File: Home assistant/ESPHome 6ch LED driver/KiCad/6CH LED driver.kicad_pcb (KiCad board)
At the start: 2 copper layers, 90 x 70 mm, 75 parts, among them J1 DC Power, J10 I2C ext, J11 UART int, J12 UART ext, J13 IO Out, J14 U Out, J2 USB_C_small, J3 LED 1, J4 LED 2, J5 LED 3, J6 LED 4, J7 LED 5, J8 LED 6, J9 I2C int, Q1 AP4409AGEM, Q2 AP4409AGEM, Q3 AO3400A, Q4 AO3400A, Q5 AO3400A, Q6 AO3400A, Q7 AO3400A, Q8 AO3400A, SW1 Reset, SW2 Boot, U1 TPS5430DDA, U2 AMS1117-3.3, U3 ESP32-C6-WROOM-1

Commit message: Fix USB
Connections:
- R4 pad 1: USB D- -> USB D+
- R5 pad 1: USB D+ -> USB D-
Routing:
- net USB D-: track 25.0 -> 17.9 mm
- net USB D+: track 21.7 -> 18.9 mm
- net IO10: track 25.2 -> 24.2 mm
- net IO11: track 27.5 -> 26.5 mm
- net Net-(U3-MTDO/GPIO7): track 16.9 -> 16.3 mm

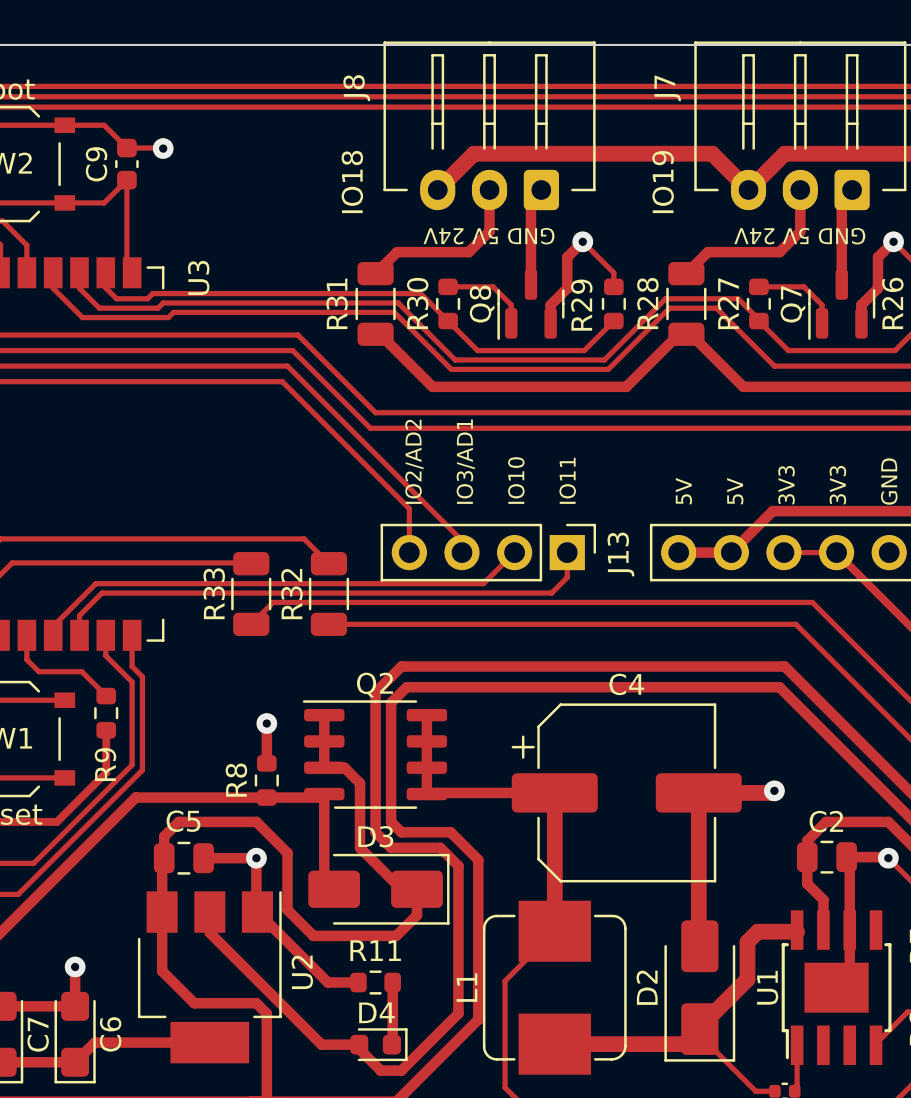
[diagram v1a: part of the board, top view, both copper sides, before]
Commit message: Fix boot mode
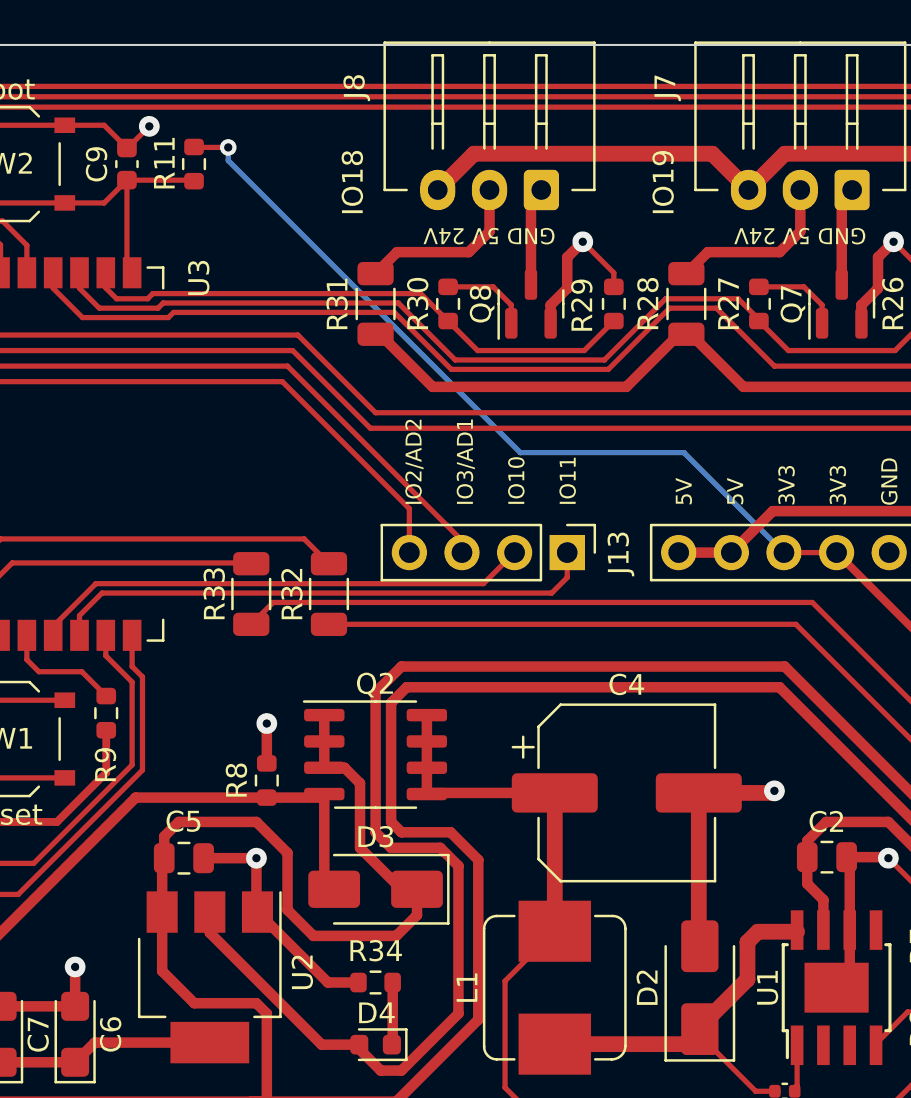
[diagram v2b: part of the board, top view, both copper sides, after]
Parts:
- added R11: 100k, Resistor_SMD:R_0603_1608Metric, F.Cu at (126.2, 68.8)
- renumbered R11 to R34
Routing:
- net +3V3: track 200.9 -> 237.9 mm, vias 0 -> 1
- net BOOT: track 14.0 -> 17.5 mm
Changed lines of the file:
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@@
     )
   )
+  (footprint "Resistor_SMD:R_0603_1608Metric" (layer "F.Cu")
+    (at 126.238 68.75 -90)
+    (descr "Resistor SMD 0603 (1608 Metric), square (rectangular) end terminal, IPC_7351 nominal, (Body size source: IPC-SM-782 page 72, https://www.pcb-3d.com/wordpress/wp-content/uploads/ipc-sm-782a_amendment_1_and_2.pdf), generated with kicad-footprint-generator")
+    (tags "resistor")
+    (property "Sheetfile" "6CH LED driver.kicad_sch")
+    (property "Sheetname" "")
+    (property "ki_description" "Resistor, small symbol")
+    (property "ki_keywords" "R resistor")
+    (attr smd)
+    (fp_text reference "R11" (at -0.043 1.397 90) (layer "F.SilkS")
+        (effects (font (size 1 1) (thickness 0.15)))
+    )
+    (fp_text value "100k" (at 0 1.43 90) (layer "F.Fab")
+        (effects (font (size 1 1) (thickness 0.15)))
+    )
+    (fp_text user "${REFERENCE}" (at 0 0 90) (layer "F.Fab")
+        (effects (font (size 0.4 0.4) (thickness 0.06)))
+    )
+    (fp_line (start -0.237258 -0.5225) (end 0.237258 -0.5225)
+      (stroke (width 0.12) (type solid)) (layer "F.SilkS"))
+    (fp_line (start -0.237258 0.5225) (end 0.237258 0.5225)
+      (stroke (width 0.12) (type solid)) (layer "F.SilkS"))
+    (fp_line (start -1.48 -0.73) (end 1.48 -0.73)
+      (stroke (width 0.05) (type solid)) (layer "F.CrtYd"))
+    (fp_line (start -1.48 0.73) (end -1.48 -0.73)
+      (stroke (width 0.05) (type solid)) (layer "F.CrtYd"))
+    (fp_line (start 1.48 -0.73) (end 1.48 0.73)
+      (stroke (width 0.05) (type solid)) (layer "F.CrtYd"))
+    (fp_line (start 1.48 0.73) (end -1.48 0.73)
+      (stroke (width 0.05) (type solid)) (layer "F.CrtYd"))
+    (fp_line (start -0.8 -0.4125) (end 0.8 -0.4125)
+      (stroke (width 0.1) (type solid)) (layer "F.Fab"))
+    (fp_line (start -0.8 0.4125) (end -0.8 -0.4125)
+      (stroke (width 0.1) (type solid)) (layer "F.Fab"))
+    (fp_line (start 0.8 -0.4125) (end 0.8 0.4125)
+      (stroke (width 0.1) (type solid)) (layer "F.Fab"))
+    (fp_line (start 0.8 0.4125) (end -0.8 0.4125)
+      (stroke (width 0.1) (type solid)) (layer "F.Fab"))
+    (pad "1" smd roundrect (at -0.825 0 270) (size 0.8 0.95) (layers "F.Cu" "F.Paste" "F.Mask") (roundrect_rratio 0.25)
+      (net 6 "+3V3") (pintype "passive"))
+    (pad "2" smd roundrect (at 0.825 0 270) (size 0.8 0.95) (layers "F.Cu" "F.Paste" "F.Mask") (roundrect_rratio 0.25)
+      (net 8 "BOOT") (pintype "passive"))
+    (model "${KICAD6_3DMODEL_DIR}/Resistor_SMD.3dshapes/R_0603_1608Metric.wrl"
+      (offset (xyz 0 0 0))
+      (scale (xyz 1 1 1))
+      (rotate (xyz 0 0 0))
+    )
+  )
   (footprint "Resistor_SMD:R_1206_3216Metric" (layer "F.Cu")
     (at 150 75.5 90)
@@
     (property "ki_keywords" "R resistor")
     (attr smd)
-    (fp_text reference "R11" (at 0 1.5) (layer "F.SilkS")
+    (fp_text reference "R34" (at 0 1.5) (layer "F.SilkS")
         (effects (font (size 1 1) (thickness 0.15)))
     )
@@
   (segment (start 117.825 116.25) (end 119.25 116.25) (width 0.254) (layer "F.Cu") (net 2))
   (segment (start 113.25 104.75) (end 112.75 105.25) (width 0.254) (layer "F.Cu") (net 2))
-  (segment (start 123 67.975) (end 124.725 67.975) (width 0.254) (layer "F.Cu") (net 2))
+  (segment (start 123.033 67.975) (end 123 67.975) (width 0.254) (layer "F.Cu") (net 2))
   (segment (start 174.25 74.75) (end 174.25 73.25) (width 0.508) (layer "F.Cu") (net 2))
   (segment (start 162.75 105.25) (end 159.75 102.25) (width 0.254) (layer "F.Cu") (net 2))
@@
   (segment (start 102 123.5) (end 104.25 123.5) (width 0.762) (layer "F.Cu") (net 2))
   (segment (start 113.71 85.5) (end 112.46 85.5) (width 0.254) (layer "F.Cu") (net 2))
-  (segment (start 124.725 67.975) (end 124.75 68) (width 0.254) (layer "F.Cu") (net 2))
   (segment (start 106.74 78.53) (end 111.21 83) (width 0.381) (layer "F.Cu") (net 2))
   (segment (start 137.55 120.45) (end 136.5 121.5) (width 0.508) (layer "F.Cu") (net 2))
@@
   (segment (start 161.5 74.675) (end 161.5 74) (width 0.254) (layer "F.Cu") (net 2))
   (segment (start 113.71 83) (end 113.71 84.25) (width 0.254) (layer "F.Cu") (net 2))
+  (segment (start 124.079 66.929) (end 123.033 67.975) (width 0.254) (layer "F.Cu") (net 2))
   (segment (start 112 96.025) (end 112 96.375) (width 0.254) (layer "F.Cu") (net 2))
   (segment (start 167.5 119.6) (end 167.5 120.5375) (width 0.508) (layer "F.Cu") (net 2))
@@
   (via (at 170.25 93) (size 1) (drill 0.4) (layers "F.Cu" "B.Cu") (net 2))
   (via (at 159.75 102.25) (size 1) (drill 0.4) (layers "F.Cu" "B.Cu") (net 2))
-  (via (at 124.75 68) (size 1) (drill 0.4) (layers "F.Cu" "B.Cu") (net 2))
+  (via (at 124.079 66.929) (size 1) (drill 0.4) (layers "F.Cu" "B.Cu") (net 2))
   (via (at 109.75 107.25) (size 1) (drill 0.4) (layers "F.Cu" "B.Cu") (net 2))
   (via (at 112.25 99.5) (size 1) (drill 0.4) (layers "F.Cu" "B.Cu") (net 2))
@@
   (segment (start 121.45 111.15) (end 120.5 112.1) (width 0.508) (layer "F.Cu") (net 6))
   (segment (start 136.25 93) (end 135 94.25) (width 0.508) (layer "F.Cu") (net 6))
+  (segment (start 126.258 67.945) (end 126.238 67.925) (width 0.254) (layer "F.Cu") (net 6))
   (segment (start 169.925 107.25) (end 172.24 107.25) (width 0.381) (layer "F.Cu") (net 6))
   (segment (start 139 102.625) (end 139 109.75) (width 0.508) (layer "F.Cu") (net 6))
@@
   (segment (start 182.5 107.25) (end 181.75 108) (width 0.381) (layer "F.Cu") (net 6))
   (segment (start 111.5 100.5) (end 119.625 100.5) (width 0.381) (layer "F.Cu") (net 6))
+  (segment (start 127.889 67.945) (end 126.258 67.945) (width 0.254) (layer "F.Cu") (net 6))
   (segment (start 169.75 101.925) (end 170.425 101.25) (width 0.381) (layer "F.Cu") (net 6))
   (segment (start 135.75 101.75) (end 138.125 101.75) (width 0.508) (layer "F.Cu") (net 6))
@@
   (segment (start 169.75 107.075) (end 169.925 107.25) (width 0.381) (layer "F.Cu") (net 6))
   (segment (start 110.25 96.075) (end 110.25 99.25) (width 0.381) (layer "F.Cu") (net 6))
+  (via (at 127.889 67.945) (size 0.8) (drill 0.4) (layers "F.Cu" "B.Cu") (net 6))
+  (segment (start 154.71 87.5) (end 149.887 82.677) (width 0.254) (layer "B.Cu") (net 6))
+  (segment (start 127.889 68.58) (end 127.889 67.945) (width 0.254) (layer "B.Cu") (net 6))
+  (segment (start 149.887 82.677) (end 141.986 82.677) (width 0.254) (layer "B.Cu") (net 6))
+  (segment (start 141.986 82.677) (end 127.889 68.58) (width 0.254) (layer "B.Cu") (net 6))
   (segment (start 110.25 94.425) (end 109.28 93.455) (width 0.254) (layer "F.Cu") (net 7))
   (segment (start 111.95 94.425) (end 112 94.475) (width 0.254) (layer "F.Cu") (net 7))
@@
   (segment (start 114 94.625) (end 120 94.625) (width 0.254) (layer "F.Cu") (net 7))
   (segment (start 121.9 70.625) (end 123 69.525) (width 0.254) (layer "F.Cu") (net 8))
+  (segment (start 123 69.525) (end 126.442 69.525) (width 0.254) (layer "F.Cu") (net 8))
   (segment (start 114 70.625) (end 120 70.625) (width 0.254) (layer "F.Cu") (net 8))
+  (segment (start 126.442 69.525) (end 126.492 69.575) (width 0.254) (layer "F.Cu") (net 8))
   (segment (start 123 69.525) (end 123 73.745) (width 0.254) (layer "F.Cu") (net 8))
   (segment (start 120 70.625) (end 121.9 70.625) (width 0.254) (layer "F.Cu") (net 8))
